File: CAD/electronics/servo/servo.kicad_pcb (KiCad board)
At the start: 2 copper layers, 17 parts, among them J1 Front ultrasound, J10 Servo7, J11 Start trigger, J2 Rear ultrasound, J3 Servo0, J4 Servo2, J5 Servo4, J6 Servo6, J7 Servo1, J8 Servo3, J9 Servo5, U1 PCF8574

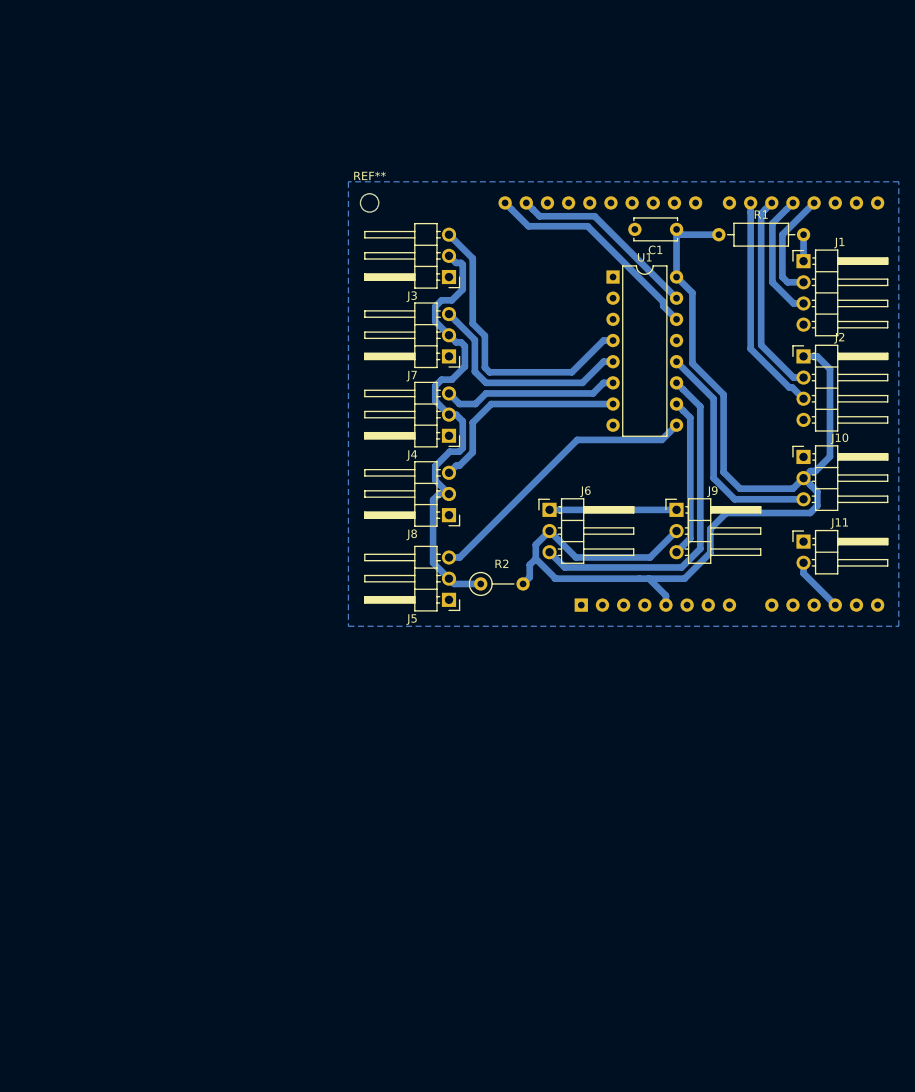
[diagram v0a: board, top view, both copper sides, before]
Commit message: Add servo board CAD design.
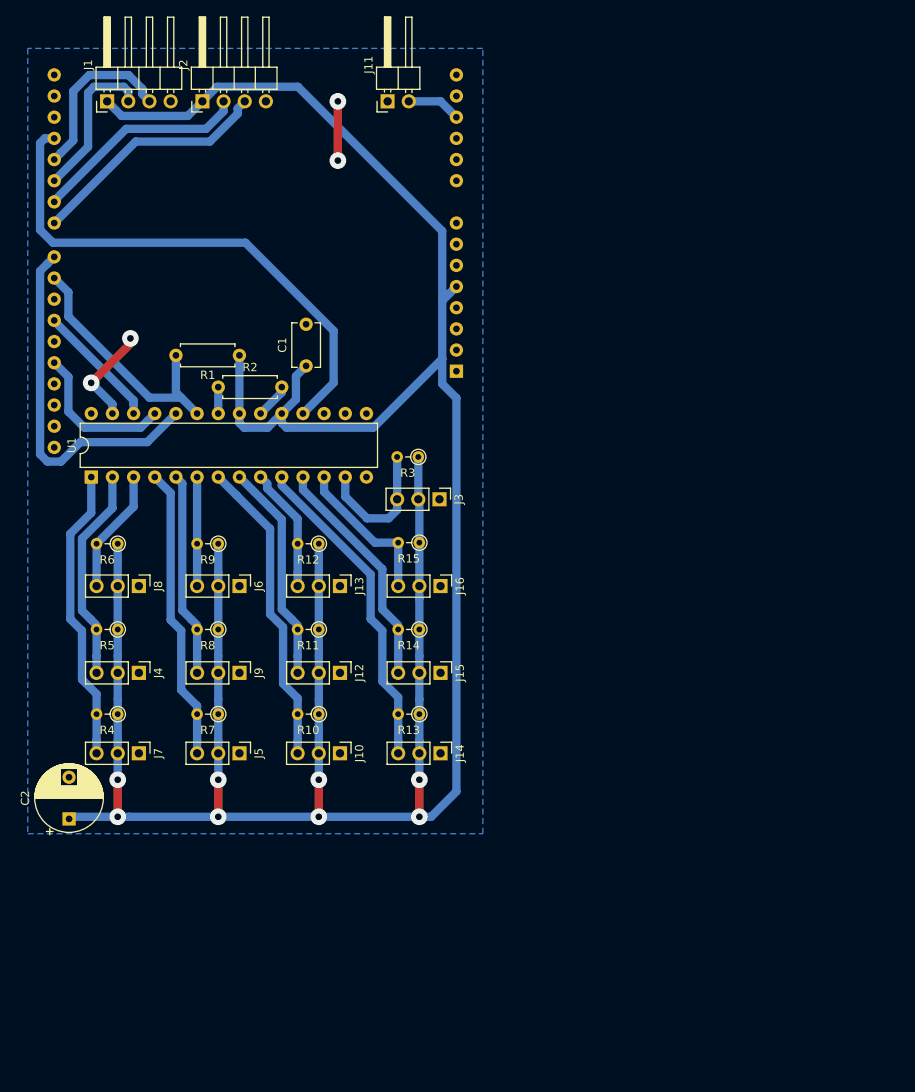
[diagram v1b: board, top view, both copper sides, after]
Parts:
- removed REF**: MountingHole_2.2mm_M2, MountingHole:MountingHole_2.2mm_M2
- added C2: CP, Capacitor_THT:CP_Radial_D8.0mm_P5.00mm, F.Cu at (24.9, 112.0)
- added J12: Servo8, Connector_PinHeader_2.54mm:PinHeader_1x03_P2.54mm_Vertical, F.Cu at (57.4, 94.5)
- added J13: Servo9, Connector_PinHeader_2.54mm:PinHeader_1x03_P2.54mm_Vertical, F.Cu at (57.4, 84.1)
- added J14: Servo10, Connector_PinHeader_2.54mm:PinHeader_1x03_P2.54mm_Vertical, F.Cu at (69.5, 104.1)
- added J15: Servo11, Connector_PinHeader_2.54mm:PinHeader_1x03_P2.54mm_Vertical, F.Cu at (69.5, 94.5)
- added J16: Servo12, Connector_PinHeader_2.54mm:PinHeader_1x03_P2.54mm_Vertical, F.Cu at (69.5, 84.1)
- added R10: R, Resistor_THT:R_Axial_DIN0204_L3.6mm_D1.6mm_P2.54mm_Vertical, F.Cu at (54.9, 99.4)
- added R11: R, Resistor_THT:R_Axial_DIN0204_L3.6mm_D1.6mm_P2.54mm_Vertical, F.Cu at (54.9, 89.3)
- added R12: R, Resistor_THT:R_Axial_DIN0204_L3.6mm_D1.6mm_P2.54mm_Vertical, F.Cu at (54.9, 79.0)
- added R13: R, Resistor_THT:R_Axial_DIN0204_L3.6mm_D1.6mm_P2.54mm_Vertical, F.Cu at (66.9, 99.4)
- added R14: R, Resistor_THT:R_Axial_DIN0204_L3.6mm_D1.6mm_P2.54mm_Vertical, F.Cu at (66.9, 89.3)
- added R15: R, Resistor_THT:R_Axial_DIN0204_L3.6mm_D1.6mm_P2.54mm_Vertical, F.Cu at (66.9, 78.9)
- added R3: R, Resistor_THT:R_Axial_DIN0204_L3.6mm_D1.6mm_P2.54mm_Vertical, F.Cu at (66.8, 68.6)
- added R4: R, Resistor_THT:R_Axial_DIN0204_L3.6mm_D1.6mm_P2.54mm_Vertical, F.Cu at (30.7, 99.4)
- added R5: R, Resistor_THT:R_Axial_DIN0204_L3.6mm_D1.6mm_P2.54mm_Vertical, F.Cu at (30.7, 89.3)
- added R6: R, Resistor_THT:R_Axial_DIN0204_L3.6mm_D1.6mm_P2.54mm_Vertical, F.Cu at (30.7, 79.0)
- added R7: R, Resistor_THT:R_Axial_DIN0204_L3.6mm_D1.6mm_P2.54mm_Vertical, F.Cu at (42.8, 99.4)
- added R8: R, Resistor_THT:R_Axial_DIN0204_L3.6mm_D1.6mm_P2.54mm_Vertical, F.Cu at (42.8, 89.3)
- added R9: R, Resistor_THT:R_Axial_DIN0204_L3.6mm_D1.6mm_P2.54mm_Vertical, F.Cu at (42.8, 79.0)
- C1: value C -> 100n; footprint Capacitor_THT:C_Disc_D5.0mm_W2.5mm_P5.00mm -> Capacitor_THT:C_Disc_D5.1mm_W3.2mm_P5.00mm
- J10, J4, J5, J6, J7, J8, J9: footprint Connector_PinHeader_2.54mm:PinHeader_1x03_P2.54mm_Horizontal -> Connector_PinHeader_2.54mm:PinHeader_1x03_P2.54mm_Vertical
- J3: value Servo0 -> Servo13; footprint Connector_PinHeader_2.54mm:PinHeader_1x03_P2.54mm_Horizontal -> Connector_PinHeader_2.54mm:PinHeader_1x03_P2.54mm_Vertical
- R1: value Wire -> 10k; footprint Resistor_THT:R_Axial_DIN0207_L6.3mm_D2.5mm_P10.16mm_Horizontal -> Resistor_THT:R_Axial_DIN0207_L6.3mm_D2.5mm_P7.62mm_Horizontal
- R2: value Wire -> 2k; footprint Resistor_THT:R_Axial_DIN0207_L6.3mm_D2.5mm_P5.08mm_Vertical -> Resistor_THT:R_Axial_DIN0207_L6.3mm_D2.5mm_P7.62mm_Horizontal
- U1: value PCF8574 -> TLC5940NT; footprint Package_DIP:DIP-16_W7.62mm -> Package_DIP:DIP-28_W7.62mm
- moved J1 85.7 mm to (29.5, 25.9), turned to 90 degrees
- moved J2 78.4 mm to (40.9, 25.9), turned to 90 degrees
- moved J11 72.7 mm to (63.1, 25.9), turned to 90 degrees
- moved U1 67.1 mm to (27.6, 71.0), turned to 90 degrees
- moved J10 66.0 mm to (57.4, 104.1), turned to 270 degrees
- moved J7 60.4 mm to (33.3, 104.1), turned to 270 degrees
- moved R1 59.3 mm to (45.3, 56.4), turned to 180 degrees
- moved J9 56.0 mm to (45.3, 94.5), turned to 270 degrees
- moved C1 47.4 mm to (53.3, 57.7), turned to 90 degrees
- moved J4 46.8 mm to (33.3, 94.5), turned to 270 degrees
- moved R2 39.4 mm to (42.8, 60.2)
- moved J6 38.3 mm to (45.3, 84.1), turned to 270 degrees
- moved J8 38.2 mm to (33.3, 84.1), turned to 270 degrees
- moved A1 31.8 mm to (71.4, 58.3), turned to 90 degrees
- moved J5 31.2 mm to (45.3, 104.1), turned to 270 degrees
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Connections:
- A1 pad 1: Net-(A1-Pad1) -> (no net)
- A1 pad 10: Net-(A1-Pad10) -> (no net)
- A1 pad 11: Net-(A1-Pad11) -> (no net)
- A1 pad 13: Net-(A1-Pad13) -> (no net)
- A1 pad 14: Net-(A1-Pad14) -> (no net)
- A1 pad 15: Net-(A1-Pad15) -> (no net)
- A1 pad 16: Net-(A1-Pad16) -> (no net)
- A1 pad 17: Net-(A1-Pad17) -> (no net)
- A1 pad 18: Net-(A1-Pad18) -> GSCLK
- A1 pad 2: Net-(A1-Pad2) -> (no net)
- A1 pad 23: Net-(A1-Pad23) -> XLAT
- A1 pad 24: Net-(A1-Pad24) -> BLANK
- A1 pad 25: Net-(A1-Pad25) -> (no net)
- A1 pad 26: Net-(A1-Pad26) -> SIN
- A1 pad 27: Net-(A1-Pad27) -> (no net)
- A1 pad 28: Net-(A1-Pad28) -> SCLK
- A1 pad 3: Net-(A1-Pad3) -> (no net)
- A1 pad 30: Net-(A1-Pad30) -> (no net)
- A1 pad 31: Net-(A1-Pad31) -> (no net)
- A1 pad 32: Net-(A1-Pad32) -> (no net)
- A1 pad 4: Net-(A1-Pad4) -> (no net)
- A1 pad 5: 5V -> +5V
- A1 pad 8: Net-(A1-Pad8) -> (no net)
- A1 pad 9: Net-(A1-Pad9) -> (no net)
- C1 pad 1: 5V -> +5V
- J1 pad 1: Net-(J1-Pad1) -> +5V
- J1 pad 2: Net-(A1-Pad18) -> Net-(A1-Pad20)
- J10 pad 2: 5V -> +5V
- J10 pad 3: Net-(J10-Pad3) -> C7
- J2 pad 1: 5V -> +5V
- J2 pad 2: Net-(A1-Pad20) -> Net-(A1-Pad21)
- J2 pad 3: Net-(A1-Pad21) -> Net-(A1-Pad22)
- J3 pad 2: Net-(J3-Pad2) -> +5V
- J3 pad 3: Net-(J3-Pad3) -> C13
- J4 pad 2: Net-(J3-Pad2) -> +5V
- J4 pad 3: Net-(J4-Pad3) -> C2
- J5 pad 2: Net-(J3-Pad2) -> +5V
- J5 pad 3: Net-(J5-Pad3) -> C4
- J6 pad 2: 5V -> +5V
- J6 pad 3: Net-(J6-Pad3) -> C6
- J7 pad 2: Net-(J3-Pad2) -> +5V
- J7 pad 3: Net-(J7-Pad3) -> C1
- J8 pad 2: Net-(J3-Pad2) -> +5V
- J8 pad 3: Net-(J8-Pad3) -> C3
- J9 pad 2: 5V -> +5V
- J9 pad 3: Net-(J9-Pad3) -> C5
- R1 pad 1: 5V -> +5V
- R1 pad 2: Net-(J1-Pad1) -> BLANK
- R2 pad 1: Net-(J3-Pad2) -> GND
- R2 pad 2: 5V -> Net-(R2-Pad2)
- U1 pad 1: GND -> C1
- U1 pad 10: Net-(J9-Pad3) -> C10
- U1 pad 11: Net-(J6-Pad3) -> C11
- U1 pad 12: Net-(J10-Pad3) -> C12
- U1 pad 13: Net-(U1-Pad13) -> C13
- U1 pad 14: Net-(A1-Pad32) -> (no net)
- U1 pad 15: Net-(A1-Pad31) -> (no net)
- U1 pad 16: 5V -> (no net)
- U1 pad 2: GND -> C2
- U1 pad 3: GND -> C3
- U1 pad 4: Net-(J3-Pad3) -> C4
- U1 pad 5: Net-(J7-Pad3) -> C5
- U1 pad 6: Net-(J4-Pad3) -> C6
- U1 pad 7: Net-(J8-Pad3) -> C7
- U1 pad 8: GND -> C8
- U1 pad 9: Net-(J5-Pad3) -> C9
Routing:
- net +5V: track 0.00 -> 352.4 mm, vias 0 -> 8
- net 5V: track 140.7 -> 0.00 mm
- net GSCLK: track 0.00 -> 64.0 mm
- net Net-(J3-Pad2): track 56.8 -> 0.00 mm
- net XLAT: track 0.00 -> 43.5 mm
- net Net-(J6-Pad3): track 40.9 -> 0.00 mm
- net C10: track 0.00 -> 38.9 mm
- net C7: track 0.00 -> 37.1 mm
- net C1: track 0.00 -> 35.7 mm
- net C4: track 0.00 -> 35.3 mm
- net Net-(J3-Pad3): track 34.9 -> 0.00 mm
- net Net-(J5-Pad3): track 33.9 -> 0.00 mm
- net BLANK: track 0.00 -> 30.9 mm
- net Net-(A1-Pad22): track 0.00 -> 29.3 mm
- net C11: track 0.00 -> 27.7 mm
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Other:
- net class Default: trace_width 0.8 -> 1; via_dia 0.8 -> 2; via_drill 0.4 -> 0.8

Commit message: Nouveau design de carte servo
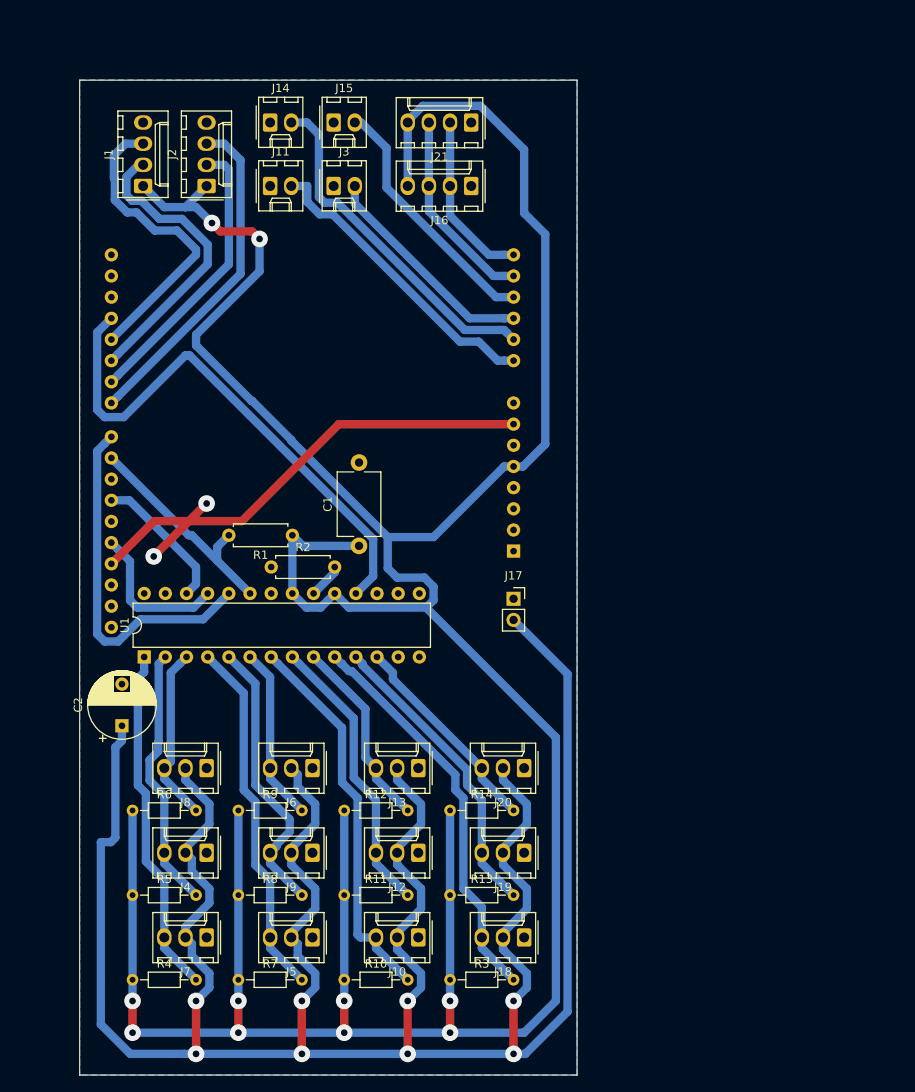
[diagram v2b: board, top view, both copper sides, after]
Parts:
- removed R15: R, Resistor_THT:R_Axial_DIN0204_L3.6mm_D1.6mm_P2.54mm_Vertical
- added J17: Servo power in, Connector_PinSocket_2.54mm:PinSocket_1x02_P2.54mm_Vertical, F.Cu at (78.2, 85.6)
- added J18: Servo10, Connector_Molex:Molex_KK-254_AE-6410-03A_1x03_P2.54mm_Vertical, F.Cu at (79.5, 126.2)
- added J19: Servo11, Connector_Molex:Molex_KK-254_AE-6410-03A_1x03_P2.54mm_Vertical, F.Cu at (79.5, 116.1)
- added J20: Servo12, Connector_Molex:Molex_KK-254_AE-6410-03A_1x03_P2.54mm_Vertical, F.Cu at (79.5, 105.9)
- added J21: I2C, Connector_Molex:Molex_KK-254_AE-6410-04A_1x04_P2.54mm_Vertical, F.Cu at (73.2, 28.4)
- C1: footprint Capacitor_THT:C_Disc_D5.1mm_W3.2mm_P5.00mm -> Capacitor_THT:C_Disc_D7.5mm_W5.0mm_P10.00mm
- J1, J2: footprint Connector_PinHeader_2.54mm:PinHeader_1x04_P2.54mm_Horizontal -> Connector_Molex:Molex_KK-254_AE-6410-04A_1x04_P2.54mm_Vertical
- J10, J12, J13, J4, J5, J6, J7, J8, J9: footprint Connector_PinHeader_2.54mm:PinHeader_1x03_P2.54mm_Vertical -> Connector_Molex:Molex_KK-254_AE-6410-03A_1x03_P2.54mm_Vertical
- J11: value Start trigger -> GPIO A0; footprint Connector_PinHeader_2.54mm:PinHeader_1x02_P2.54mm_Horizontal -> Connector_Molex:Molex_KK-254_AE-6410-02A_1x02_P2.54mm_Vertical
- J14: value Servo10 -> GPIO A1; footprint Connector_PinHeader_2.54mm:PinHeader_1x03_P2.54mm_Vertical -> Connector_Molex:Molex_KK-254_AE-6410-02A_1x02_P2.54mm_Vertical
- J15: value Servo11 -> GPIO A3; footprint Connector_PinHeader_2.54mm:PinHeader_1x03_P2.54mm_Vertical -> Connector_Molex:Molex_KK-254_AE-6410-02A_1x02_P2.54mm_Vertical
- J16: value Servo12 -> I2C; footprint Connector_PinHeader_2.54mm:PinHeader_1x03_P2.54mm_Vertical -> Connector_Molex:Molex_KK-254_AE-6410-04A_1x04_P2.54mm_Vertical
- J3: value Servo13 -> GPIO A2; footprint Connector_PinHeader_2.54mm:PinHeader_1x03_P2.54mm_Vertical -> Connector_Molex:Molex_KK-254_AE-6410-02A_1x02_P2.54mm_Vertical
- R10, R11, R12, R13, R14, R3, R4, R5, R6, R7, R8, R9: footprint Resistor_THT:R_Axial_DIN0204_L3.6mm_D1.6mm_P2.54mm_Vertical -> Resistor_THT:R_Axial_DIN0204_L3.6mm_D1.6mm_P7.62mm_Horizontal
- moved J14 78.4 mm to (49.0, 28.4), turned to 0 degrees
- moved J15 67.3 mm to (56.6, 28.4), turned to 0 degrees
- moved R3 62.9 mm to (70.6, 131.3), turned to 0 degrees
- moved J16 48.1 mm to (73.2, 36.1), turned to 180 degrees
- moved J3 39.7 mm to (56.6, 36.1), turned to 0 degrees
- moved R12 32.1 mm to (57.9, 111.0), turned to 0 degrees
- moved R9 32.1 mm to (45.2, 111.0), turned to 0 degrees
- moved R6 32.1 mm to (32.5, 111.0), turned to 0 degrees
- moved R10 32.0 mm to (57.9, 131.3), turned to 0 degrees
- moved R11 32.0 mm to (57.9, 121.2), turned to 0 degrees
- moved R7 32.0 mm to (45.2, 131.3), turned to 0 degrees
- moved R8 32.0 mm to (45.2, 121.2), turned to 0 degrees
- moved R4 31.9 mm to (32.5, 131.3), turned to 0 degrees
- moved R5 31.9 mm to (32.5, 121.2), turned to 0 degrees
- moved J10 24.0 mm to (66.8, 126.2), turned to 180 degrees
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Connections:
- A1 pad 1: (no net) -> Net-(A1-Pad1)
- A1 pad 10: (no net) -> ARDUINO_A1
- A1 pad 11: (no net) -> ARDUINO_A2
- A1 pad 12: Net-(A1-Pad12) -> ARDUINO_A3
- A1 pad 13: (no net) -> SDA
- A1 pad 14: (no net) -> SCL
- A1 pad 15: (no net) -> Net-(A1-Pad15)
- A1 pad 16: (no net) -> Net-(A1-Pad16)
- A1 pad 17: (no net) -> Net-(A1-Pad17)
- A1 pad 2: (no net) -> Net-(A1-Pad2)
- A1 pad 25: (no net) -> Net-(A1-Pad25)
- A1 pad 27: (no net) -> Net-(A1-Pad27)
- A1 pad 3: (no net) -> Net-(A1-Pad3)
- A1 pad 30: (no net) -> Net-(A1-Pad30)
- A1 pad 31: (no net) -> Net-(A1-Pad31)
- A1 pad 32: (no net) -> Net-(A1-Pad32)
- A1 pad 4: (no net) -> Net-(A1-Pad4)
- A1 pad 8: (no net) -> Net-(A1-Pad8)
- A1 pad 9: (no net) -> ARDUINO_A0
- C2 pad 1: +5V -> 5V_SERVO
- J10 pad 2: +5V -> 5V_SERVO
- J11 pad 2: Net-(A1-Pad12) -> ARDUINO_A0
- J12 pad 2: +5V -> 5V_SERVO
- J13 pad 2: +5V -> 5V_SERVO
- J14 pad 2: +5V -> ARDUINO_A1
- J15 pad 2: +5V -> ARDUINO_A3
- J16 pad 2: +5V -> SCL
- J16 pad 3: C12 -> SDA
- J3 pad 2: +5V -> ARDUINO_A2
- J4 pad 2: +5V -> 5V_SERVO
- J5 pad 2: +5V -> 5V_SERVO
- J6 pad 2: +5V -> 5V_SERVO
- J7 pad 2: +5V -> 5V_SERVO
- J8 pad 2: +5V -> 5V_SERVO
- J9 pad 2: +5V -> 5V_SERVO
- R13 pad 2: C10 -> CB
- R14 pad 2: C11 -> CC
- R3 pad 2: C13 -> CA
- U1 pad 10: C10 -> CA
- U1 pad 11: C11 -> CB
- U1 pad 12: C12 -> CC
- U1 pad 13: C13 -> Net-(U1-Pad13)
- U1 pad 14: (no net) -> Net-(U1-Pad14)
- U1 pad 15: (no net) -> Net-(U1-Pad15)
- U1 pad 16: (no net) -> Net-(U1-Pad16)
- U1 pad 17: (no net) -> Net-(U1-Pad17)
- U1 pad 28: (no net) -> Net-(U1-Pad28)
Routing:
- net 5V_SERVO: track 0.00 -> 310.4 mm, vias 0 -> 8
- net +5V: track 352.4 -> 412.7 mm, vias 8 -> 10
- net CA: track 0.00 -> 47.8 mm
- net GND: track 22.3 -> 64.2 mm, vias 4 -> 2
- net ARDUINO_A1: track 0.00 -> 41.9 mm
- net C10: track 38.9 -> 0.00 mm
- net ARDUINO_A0: track 0.00 -> 36.5 mm
- net CB: track 0.00 -> 36.4 mm
- net ARDUINO_A3: track 0.00 -> 30.5 mm
- net C11: track 27.7 -> 0.00 mm
- net ARDUINO_A2: track 0.00 -> 26.9 mm
- net CC: track 0.00 -> 25.2 mm
- net SDA: track 0.00 -> 24.0 mm
- net SCL: track 0.00 -> 20.8 mm
- net C12: track 18.4 -> 0.00 mm
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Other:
- board outline added: 59.7 x 119.4 mm
